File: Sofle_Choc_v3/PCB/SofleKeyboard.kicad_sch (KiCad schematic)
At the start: 93 parts, among them J1 4PIN, J2 OLED, J3 nice!view, J4 B+, J5 B-, SW1 SW_PUSH_LED, SW10 SW_PUSH_LED, SW11 SW_PUSH_LED, SW12 SW_PUSH_LED, SW13 SW_PUSH_LED, SW14 SW_PUSH_LED, SW15 SW_PUSH_LED, SW16 SW_PUSH_LED, SW17 SW_PUSH_LED, SW18 SW_PUSH_LED, SW19 SW_PUSH_LED, SW2 SW_PUSH_LED, SW20 SW_PUSH_LED, SW21 SW_PUSH_LED, SW22 SW_PUSH_LED, SW23 SW_PUSH_LED, SW24 SW_PUSH_LED, SW25 Rotary_Encoder_Switch, SW26 SW_PUSH_LED, SW27 SW_PUSH_LED, SW28 SW_PUSH_LED, SW29 SW_PUSH_LED, SW3 SW_PUSH_LED, SW30 SW_PUSH_LED, SW31 PWR Top, SW32 PWR Bottom, SW4 SW_PUSH_LED, SW5 SW_PUSH_LED, SW6 SW_PUSH_LED, SW7 SW_PUSH_LED, SW8 SW_PUSH_LED, SW9 SW_PUSH_LED, U1 ProMicro

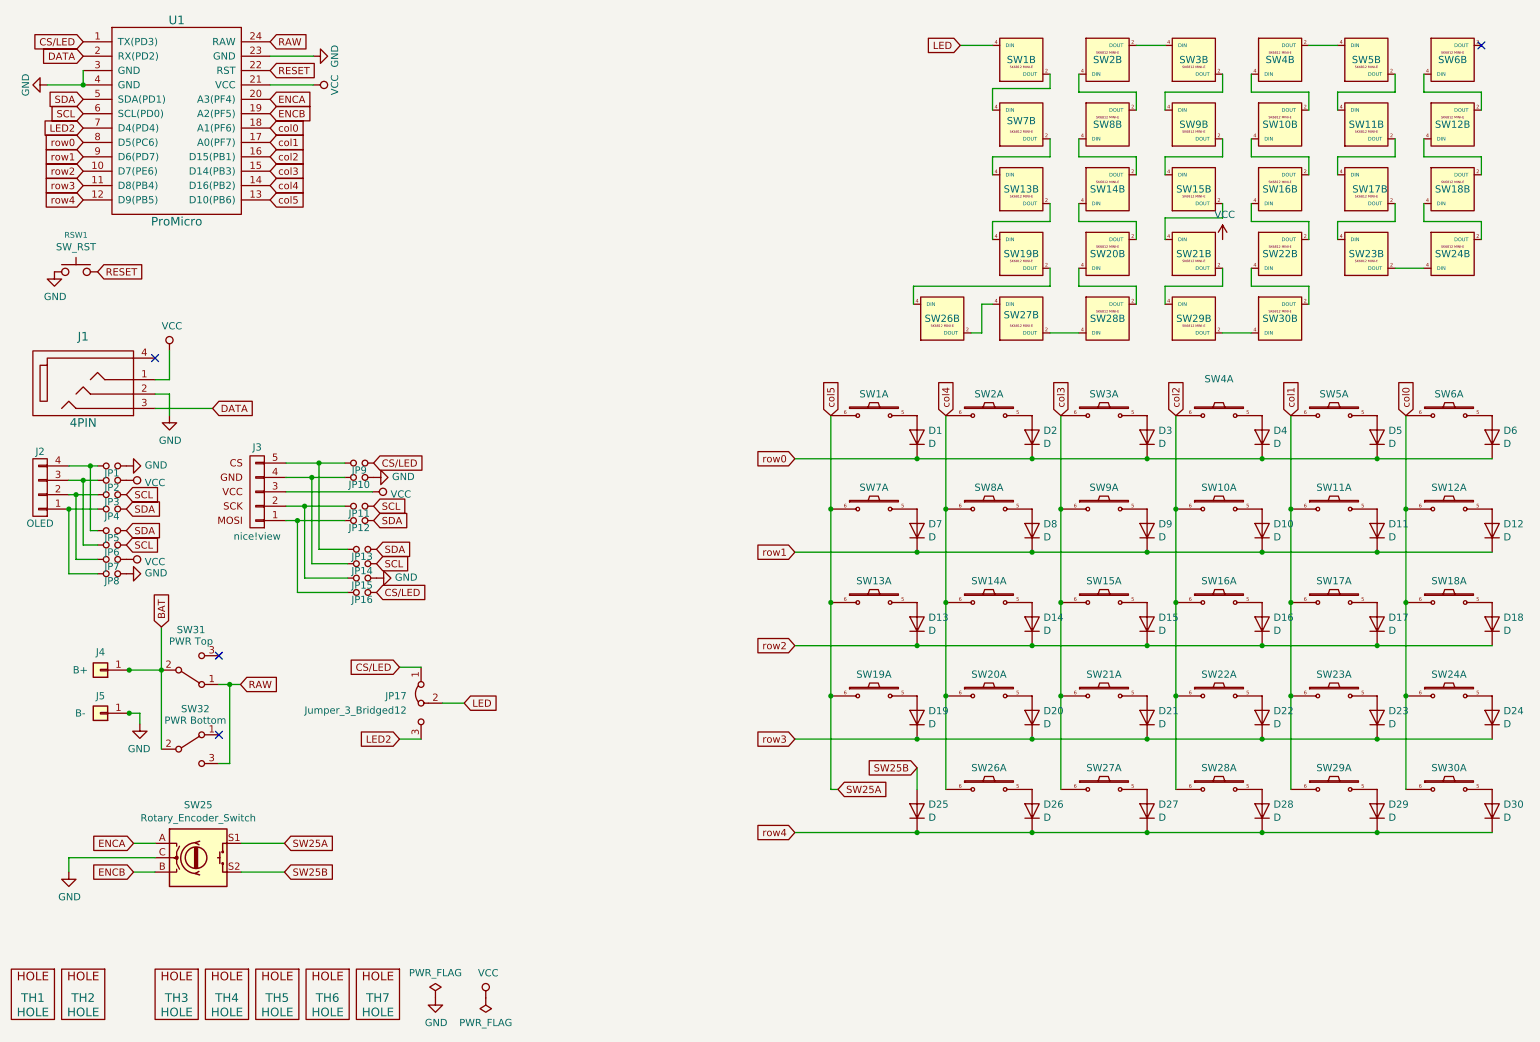
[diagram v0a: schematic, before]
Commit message: Sofle Choc: add support for extra switch instead of encoder
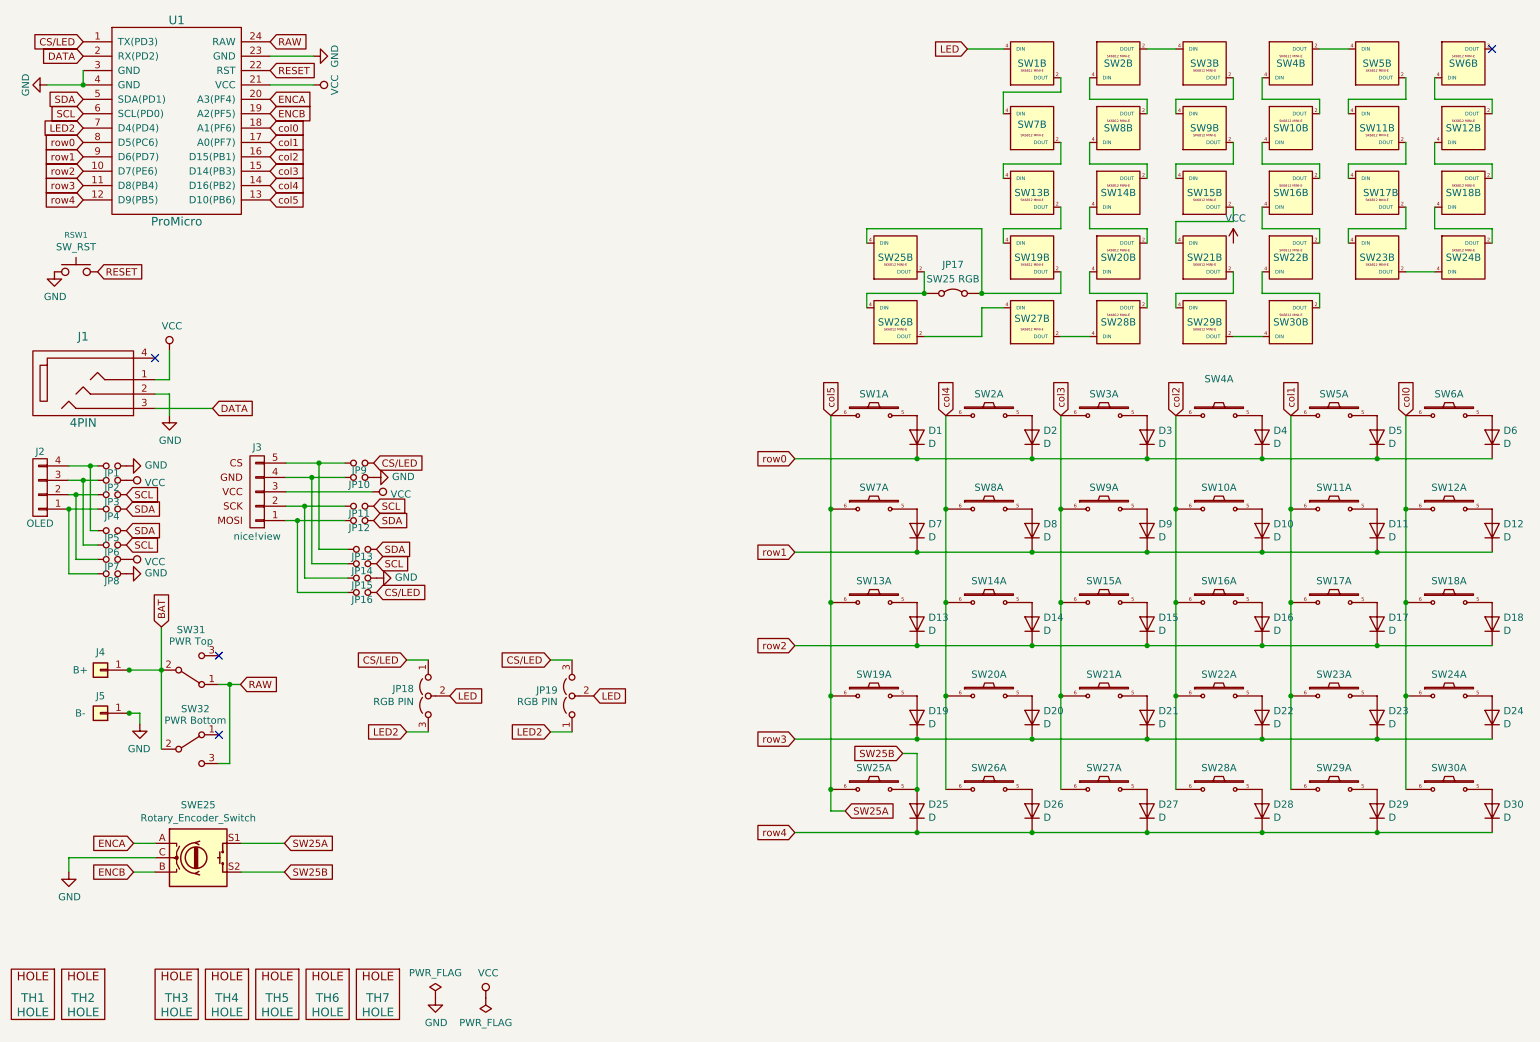
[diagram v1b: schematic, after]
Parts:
- removed JP17: Jumper_3_Bridged12, Jumper:SolderJumper-3_P1.3mm_Bridged12_RoundedPad1.0x1.5mm_NumberLabels, symbol Jumper:Jumper_3_Bridged12
- added JP17: SW25 RGB, Jumper:SolderJumper-2_P1.3mm_Bridged_RoundedPad1.0x1.5mm, symbol Jumper:Jumper_2_Bridged
- added JP18, JP19: RGB PIN, Jumper:SolderJumper-3_P1.3mm_Open_RoundedPad1.0x1.5mm, symbol Jumper:Jumper_3_Open
- added SW25: SW_PUSH_LED, SofleChoc:Choc_Hotswap_SK6812MiniE_alt_pads_w_cutouts, symbol SofleKeyboard:SW_PUSH_LED
- D1, D10, D11, D12, D13, D14, D15, D16, D17, D18, D19, D2, D20, D21, D22, D23, D24, D25, D26, D27, D28, D29, D3, D30, D4, D5, D6, D7, D8, D9: footprint SofleChoc:crkbd-diode -> SofleChoc:SOD-123_with_cutout
- J1: footprint SofleChoc:MJ-4PP-9 -> SofleChoc:PJ-320A_double_sided_with_cutouts
- J2: footprint SofleChoc:OLED_4Pin -> SofleChoc:OLED_4Pin_with_cutouts
- J3: footprint SofleChoc:niceview_5Pin -> SofleChoc:niceview_5Pin_with_cutouts
- J4: footprint Connector_PinHeader_2.54mm:PinHeader_1x01_P2.54mm_Vertical -> SofleChoc:PinHeader_1x01_P2.54mm_Vertical_B+
- J5: footprint Connector_PinHeader_2.54mm:PinHeader_1x01_P2.54mm_Vertical -> SofleChoc:PinHeader_1x01_P2.54mm_Vertical_B-
- RSW1: footprint SofleChoc:TACT_SWITCH_TVBP06 -> SofleChoc:TACT_SWITCH_TVBP06_with_cutouts
- SW1, SW10, SW11, SW12, SW13, SW14, SW15, SW16, SW17, SW18, SW19, SW2, SW20, SW21, SW22, SW23, SW24, SW26, SW27, SW28, SW29, SW3, SW30, SW4, SW5, SW6, SW7, SW8, SW9: footprint SofleChoc:Choc_Hotswap_SK6812MiniE -> SofleChoc:Choc_Hotswap_SK6812MiniE_with_cutouts
- U1: footprint SofleChoc:ProMicro -> SofleChoc:ProMicro_with_cutouts
- renumbered SW25 to SWE25
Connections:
- net CS/LED: now also JP18.1 (A), JP19.3 (B)
- net GND: now also SW25.3 (GND)
- net LED: now also JP18.2 (C), JP19.2 (C)
- net LED2: now also JP18.3 (B), JP19.1 (A)
- net SW25A: now also SW25.6
- net SW25B: now also SW25.5
- net VCC: now also SW25.1 (VDD)
- net at SW19.2 (DOUT): now also JP17.2 (B), SW25.4 (DIN); no longer SW26.4 (DIN)
- new net: JP17.1 (A), SW25.2 (DOUT), SW26.4 (DIN)
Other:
- moved on the sheet: SW10B, SW11B, SW12B, SW13B, SW14B, SW15B, SW16B, SW17B, SW18B, SW19B, SW1B, SW20B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
